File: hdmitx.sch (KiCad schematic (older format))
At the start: 38 parts, among them J21 I2C_BCK, J22 I2C_WS, J23 I2C_DATA, J24 I2C_MCLK, J4 HDMI_CONN, U15 TLV70018, U16 TLV70018, U3 IT6613

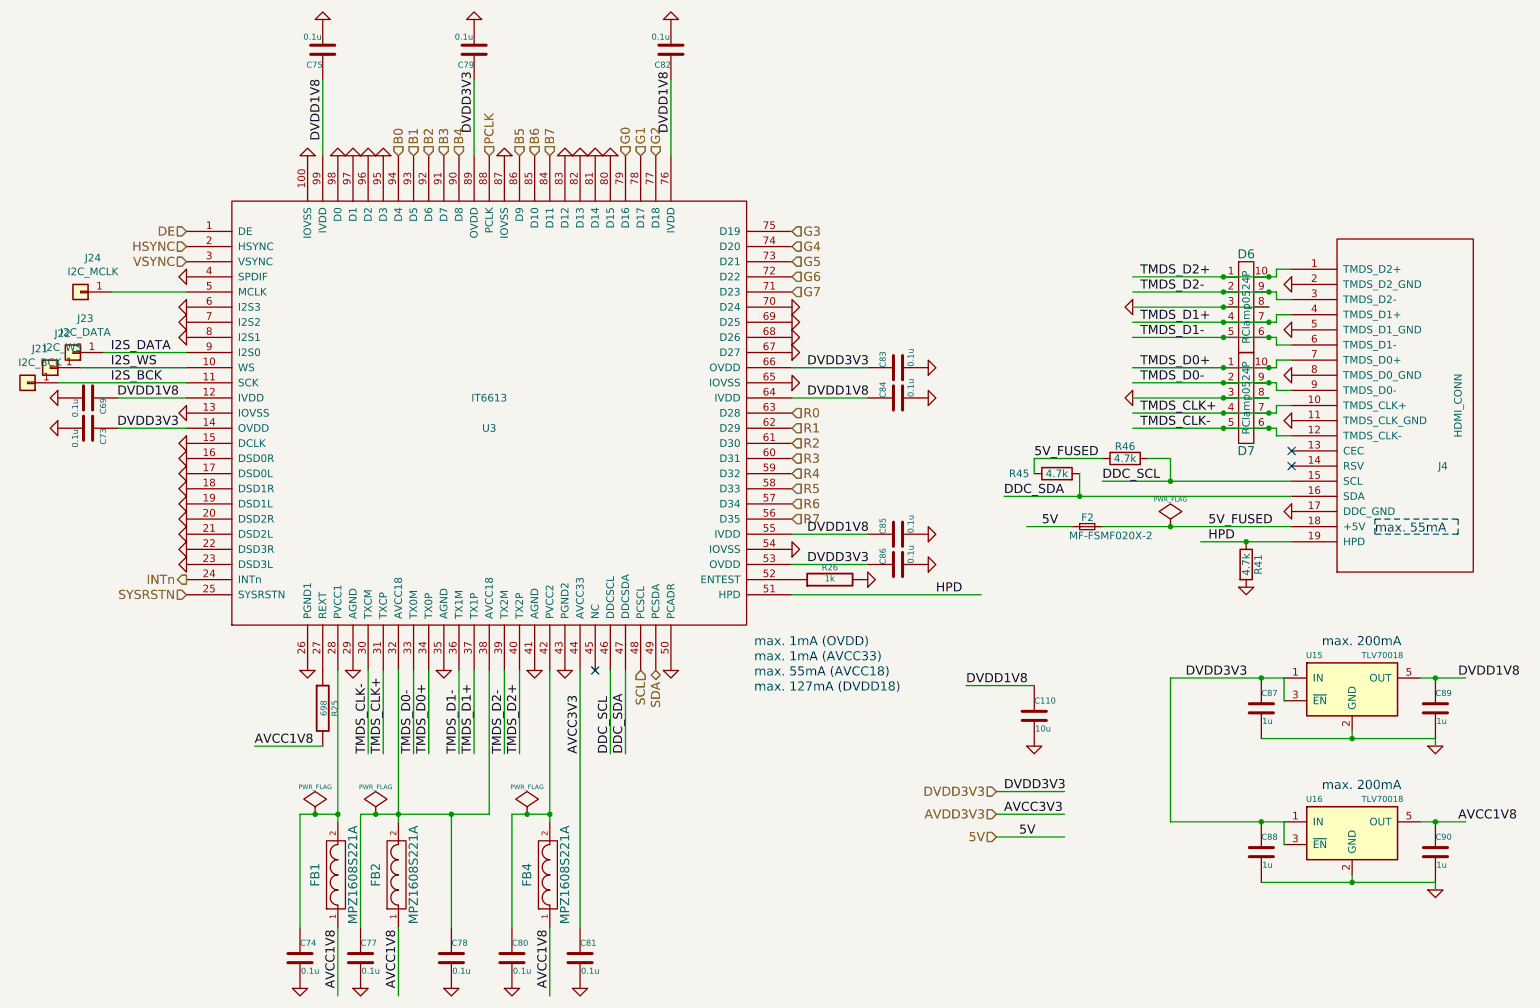
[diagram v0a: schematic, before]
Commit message: NeXT Sound Box function (1st rev) (#1)
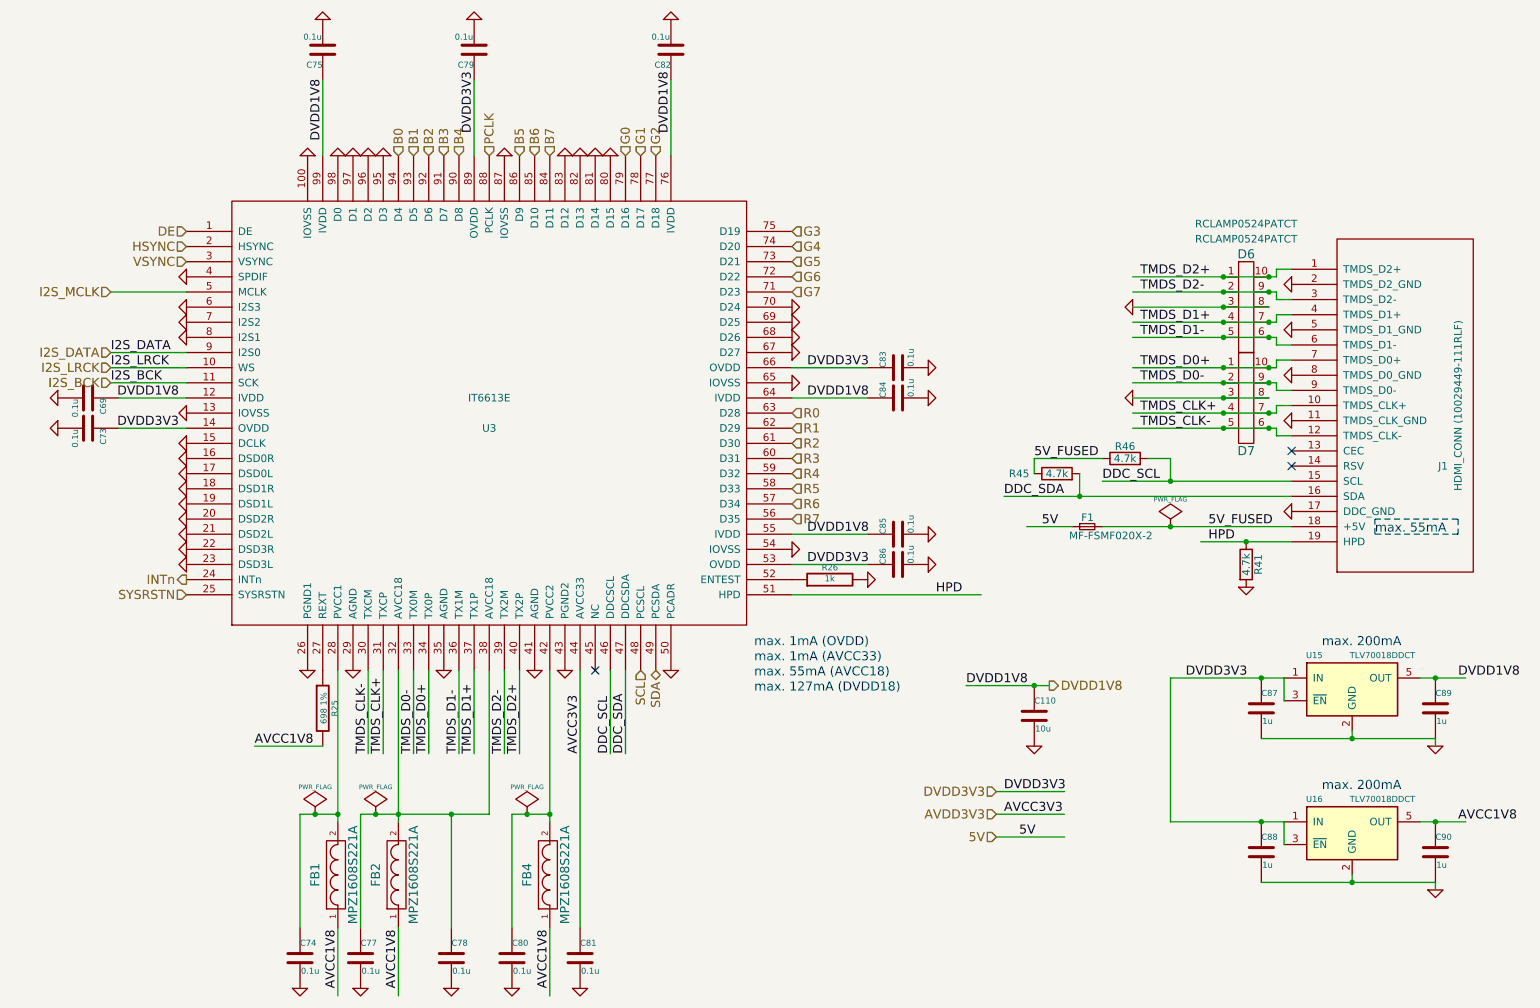
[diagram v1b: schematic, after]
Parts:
- removed J21: I2C_BCK, custom_components:TestPad-D1.0mm, symbol Connector_Generic:Conn_01x01
- removed J22: I2C_WS, custom_components:TestPad-D1.0mm, symbol Connector_Generic:Conn_01x01
- removed J23: I2C_DATA, custom_components:TestPad-D1.0mm, symbol Connector_Generic:Conn_01x01
- removed J24: I2C_MCLK, custom_components:TestPad-D1.0mm, symbol Connector_Generic:Conn_01x01
- C110, C69, C73, C74, C75, C77, C78, C79, C80, C81, C82, C83, C84, C85, C86, C87, C88, C89, C90: footprint custom_components:SM0603_Capa_libcms -> Capacitor_SMD:C_0603_1608Metric_Pad1.05x0.95mm_HandSolder
- D6, D7: value RClamp0524P -> RCLAMP0524PATCT
- F1: renamed from F2; footprint custom_components:SM0603_Resistor_libcms -> Inductor_SMD:L_0603_1608Metric_Pad1.05x0.95mm_HandSolder
- FB1, FB2, FB4: footprint custom_components:SM0603_Resistor_libcms -> Inductor_SMD:L_0603_1608Metric_Pad1.05x0.95mm_HandSolder
- J1: renamed from J4; value HDMI_CONN -> HDMI_CONN (10029449-111RLF)
- R25: value 698 -> 698 1%; footprint custom_components:SM0603_Resistor_libcms -> Resistor_SMD:R_0603_1608Metric_Pad1.05x0.95mm_HandSolder
- R26, R41, R45, R46: footprint custom_components:SM0603_Resistor_libcms -> Resistor_SMD:R_0603_1608Metric_Pad1.05x0.95mm_HandSolder
- U15, U16: value TLV70018 -> TLV70018DDCT
- U3: value IT6613 -> IT6613E
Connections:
- net labels added: I2S_LRCK, I2S_MCLK
- net labels removed: I2S_WS
- wire segments 129 -> 130
